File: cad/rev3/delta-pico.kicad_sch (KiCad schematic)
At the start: 69 parts, among them J1 Conn_01x02, J2 Conn_01x14, J3 Conn_01x04, J4 Conn_01x04, SW1 SW_SPDT, SW10 SW_Push, SW11 SW_Push, SW12 SW_Push, SW13 SW_Push, SW14 SW_Push, SW15 SW_Push, SW16 SW_Push, SW17 SW_Push, SW18 SW_Push, SW19 SW_Push, SW2 SW_Push, SW20 SW_Push, SW21 SW_Push, SW22 SW_Push, SW23 SW_Push, SW24 SW_Push, SW25 SW_Push, SW26 SW_Push, SW27 SW_Push, SW28 SW_Push, SW29 SW_Push, SW3 SW_Push, SW30 SW_Push, SW31 SW_Push, SW4 SW_Push, SW5 SW_Push, SW6 SW_Push, SW7 SW_Push, SW8 SW_Push, SW9 SW_Push, U1 PCF8574A, U2 PCF8574A, U3 Pico, U4 24LC16

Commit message: Fix footprint for new relative library path
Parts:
- U?: renamed from U3; footprint MCU_RaspberryPi_and_Boards:RPi_Pico_SMD -> RPi_Pico:RPi_Pico_SMD_TH
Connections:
- net 3V3: now also U?.36 (3V3)
- net CS: now also U?.6 (GPIO4)
- net DC: now also U?.7 (GPIO5)
- net DISPLAY_RESET: now also U?.9 (GPIO6)
- net GND: now also U?.3 (GND)
- net SCK: now also U?.4 (GPIO2)
- net SCL: now also U?.27 (GPIO21)
- net SDA: now also U?.26 (GPIO20)
- net SDI: now also U?.5 (GPIO3)
- net SDO: now also U?.1 (GPIO0)
- net SD_CS: now also U?.34 (GPIO28_ADC2)
- net VIN: now also U?.39 (VSYS)

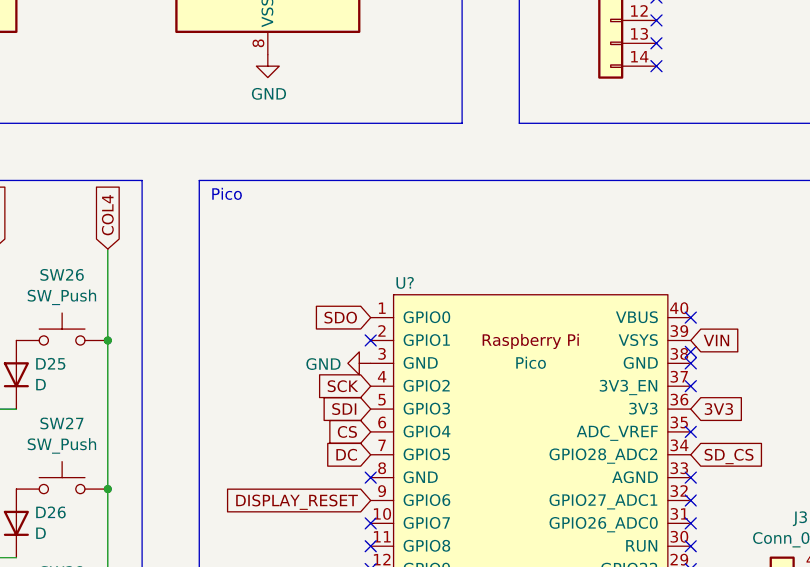
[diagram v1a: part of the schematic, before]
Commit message: Remove through-hole stuff from footprint, update board
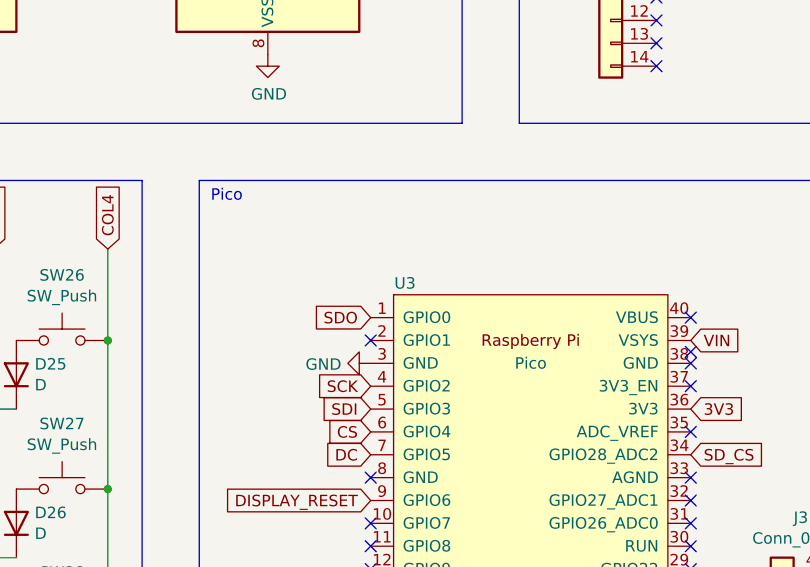
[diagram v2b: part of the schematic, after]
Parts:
- gave numbers to parts that had none: 1
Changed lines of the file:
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@@
 (kicad_sch (version 20210621) (generator eeschema)
   (paper "A4")
+  (junction (at 35.56 102.87) (diameter 0) (color 0 0 0 0))
+  (junction (at 45.72 128.27) (diameter 0) (color 0 0 0 0))
   (junction (at 48.26 168.91) (diameter 0) (color 0 0 0 0))
+  (junction (at 73.66 185.42) (diameter 0) (color 0 0 0 0))
+  (junction (at 48.26 185.42) (diameter 0) (color 0 0 0 0))
+  (junction (at 83.82 111.76) (diameter 0) (color 0 0 0 0))
+  (junction (at 45.72 144.78) (diameter 0) (color 0 0 0 0))
+  (junction (at 35.56 152.4) (diameter 0) (color 0 0 0 0))
+  (junction (at 45.72 111.76) (diameter 0) (color 0 0 0 0))
+  (junction (at 35.56 135.89) (diameter 0) (color 0 0 0 0))
+  (junction (at 48.26 102.87) (diameter 0) (color 0 0 0 0))
+  (junction (at 71.12 95.25) (diameter 0) (color 0 0 0 0))
+  (junction (at 45.72 95.25) (diameter 0) (color 0 0 0 0))
+  (junction (at 58.42 128.27) (diameter 0) (color 0 0 0 0))
+  (junction (at 73.66 152.4) (diameter 0) (color 0 0 0 0))
+  (junction (at 60.96 135.89) (diameter 0) (color 0 0 0 0))
+  (junction (at 73.66 102.87) (diameter 0) (color 0 0 0 0))
+  (junction (at 73.66 168.91) (diameter 0) (color 0 0 0 0))
+  (junction (at 58.42 111.76) (diameter 0) (color 0 0 0 0))
+  (junction (at 60.96 168.91) (diameter 0) (color 0 0 0 0))
+  (junction (at 96.52 95.25) (diameter 0) (color 0 0 0 0))
+  (junction (at 58.42 95.25) (diameter 0) (color 0 0 0 0))
+  (junction (at 48.26 119.38) (diameter 0) (color 0 0 0 0))
+  (junction (at 96.52 144.78) (diameter 0) (color 0 0 0 0))
+  (junction (at 45.72 161.29) (diameter 0) (color 0 0 0 0))
+  (junction (at 73.66 119.38) (diameter 0) (color 0 0 0 0))
+  (junction (at 119.38 170.18) (diameter 0) (color 0 0 0 0))
   (junction (at 83.82 161.29) (diameter 0) (color 0 0 0 0))
-  (junction (at 35.56 135.89) (diameter 0) (color 0 0 0 0))
+  (junction (at 48.26 152.4) (diameter 0) (color 0 0 0 0))
+  (junction (at 71.12 128.27) (diameter 0) (color 0 0 0 0))
+  (junction (at 96.52 161.29) (diameter 0) (color 0 0 0 0))
+  (junction (at 58.42 144.78) (diameter 0) (color 0 0 0 0))
+  (junction (at 83.82 95.25) (diameter 0) (color 0 0 0 0))
+  (junction (at 60.96 152.4) (diameter 0) (color 0 0 0 0))
+  (junction (at 71.12 111.76) (diameter 0) (color 0 0 0 0))
+  (junction (at 60.96 185.42) (diameter 0) (color 0 0 0 0))
+  (junction (at 58.42 161.29) (diameter 0) (color 0 0 0 0))
+  (junction (at 60.96 102.87) (diameter 0) (color 0 0 0 0))
+  (junction (at 96.52 111.76) (diameter 0) (color 0 0 0 0))
+  (junction (at 96.52 128.27) (diameter 0) (color 0 0 0 0))
+  (junction (at 71.12 144.78) (diameter 0) (color 0 0 0 0))
+  (junction (at 73.66 135.89) (diameter 0) (color 0 0 0 0))
+  (junction (at 71.12 161.29) (diameter 0) (color 0 0 0 0))
+  (junction (at 60.96 45.72) (diameter 0) (color 0 0 0 0))
+  (junction (at 35.56 185.42) (diameter 0) (color 0 0 0 0))
+  (junction (at 60.96 119.38) (diameter 0) (color 0 0 0 0))
+  (junction (at 60.96 48.26) (diameter 0) (color 0 0 0 0))
+  (junction (at 48.26 135.89) (diameter 0) (color 0 0 0 0))
   (junction (at 83.82 144.78) (diameter 0) (color 0 0 0 0))
-  (junction (at 73.66 185.42) (diameter 0) (color 0 0 0 0))
-  (junction (at 73.66 102.87) (diameter 0) (color 0 0 0 0))
-  (junction (at 58.42 128.27) (diameter 0) (color 0 0 0 0))
   (junction (at 83.82 128.27) (diameter 0) (color 0 0 0 0))
-  (junction (at 96.52 144.78) (diameter 0) (color 0 0 0 0))
-  (junction (at 35.56 185.42) (diameter 0) (color 0 0 0 0))
-  (junction (at 45.72 95.25) (diameter 0) (color 0 0 0 0))
-  (junction (at 35.56 102.87) (diameter 0) (color 0 0 0 0))
-  (junction (at 83.82 95.25) (diameter 0) (color 0 0 0 0))
-  (junction (at 96.52 161.29) (diameter 0) (color 0 0 0 0))
-  (junction (at 73.66 119.38) (diameter 0) (color 0 0 0 0))
-  (junction (at 60.96 102.87) (diameter 0) (color 0 0 0 0))
-  (junction (at 48.26 135.89) (diameter 0) (color 0 0 0 0))
-  (junction (at 60.96 168.91) (diameter 0) (color 0 0 0 0))
-  (junction (at 48.26 152.4) (diameter 0) (color 0 0 0 0))
-  (junction (at 71.12 111.76) (diameter 0) (color 0 0 0 0))
-  (junction (at 45.72 161.29) (diameter 0) (color 0 0 0 0))
   (junction (at 35.56 168.91) (diameter 0) (color 0 0 0 0))
-  (junction (at 58.42 161.29) (diameter 0) (color 0 0 0 0))
-  (junction (at 96.52 128.27) (diameter 0) (color 0 0 0 0))
-  (junction (at 60.96 135.89) (diameter 0) (color 0 0 0 0))
-  (junction (at 71.12 95.25) (diameter 0) (color 0 0 0 0))
-  (junction (at 48.26 119.38) (diameter 0) (color 0 0 0 0))
-  (junction (at 73.66 152.4) (diameter 0) (color 0 0 0 0))
   (junction (at 35.56 119.38) (diameter 0) (color 0 0 0 0))
-  (junction (at 73.66 135.89) (diameter 0) (color 0 0 0 0))
-  (junction (at 58.42 95.25) (diameter 0) (color 0 0 0 0))
-  (junction (at 35.56 152.4) (diameter 0) (color 0 0 0 0))
-  (junction (at 58.42 111.76) (diameter 0) (color 0 0 0 0))
-  (junction (at 119.38 170.18) (diameter 0) (color 0 0 0 0))
-  (junction (at 71.12 144.78) (diameter 0) (color 0 0 0 0))
-  (junction (at 58.42 144.78) (diameter 0) (color 0 0 0 0))
-  (junction (at 96.52 95.25) (diameter 0) (color 0 0 0 0))
-  (junction (at 45.72 128.27) (diameter 0) (color 0 0 0 0))
-  (junction (at 71.12 161.29) (diameter 0) (color 0 0 0 0))
-  (junction (at 48.26 185.42) (diameter 0) (color 0 0 0 0))
-  (junction (at 96.52 111.76) (diameter 0) (color 0 0 0 0))
-  (junction (at 60.96 48.26) (diameter 0) (color 0 0 0 0))
-  (junction (at 45.72 144.78) (diameter 0) (color 0 0 0 0))
-  (junction (at 60.96 45.72) (diameter 0) (color 0 0 0 0))
-  (junction (at 60.96 152.4) (diameter 0) (color 0 0 0 0))
-  (junction (at 83.82 111.76) (diameter 0) (color 0 0 0 0))
-  (junction (at 48.26 102.87) (diameter 0) (color 0 0 0 0))
-  (junction (at 60.96 119.38) (diameter 0) (color 0 0 0 0))
-  (junction (at 73.66 168.91) (diameter 0) (color 0 0 0 0))
-  (junction (at 71.12 128.27) (diameter 0) (color 0 0 0 0))
-  (junction (at 60.96 185.42) (diameter 0) (color 0 0 0 0))
-  (junction (at 45.72 111.76) (diameter 0) (color 0 0 0 0))
   (no_connect (at 161.29 113.03))
   (no_connect (at 161.29 120.65))
@@
   (symbol (lib_id "MCU_RaspberryPi_and_Boards:Pico") (at 143.51 116.84 0) (unit 1)
     (in_bom yes) (on_board yes)
-    (property "Reference" "U?" (id 0) (at 129.54 88.9 0))
+    (property "Reference" "U3" (id 0) (at 129.54 88.9 0))
     (property "Value" "Pico" (id 1) (at 143.51 97.79 0))
     (property "Footprint" "RPi_Pico:RPi_Pico_SMD_TH" (id 2) (at 143.51 116.84 90)
@@
   (symbol (lib_id "power:GND") (at 176.53 123.19 90) (unit 1)
     (in_bom yes) (on_board yes)
-    (property "Reference" "#PWR?" (id 0) (at 182.88 123.19 0)
+    (property "Reference" "#PWR0101" (id 0) (at 182.88 123.19 0)
       (effects (font (size 1.27 1.27)) hide)
     )
@@
       (reference "#PWR03") (unit 1) (value "GND") (footprint "")
     )
+    (path "/00000000-0000-0000-0000-0000613d20c7"
+      (reference "#PWR0101") (unit 1) (value "GND") (footprint "")
+    )
     (path "/00000000-0000-0000-0000-0000610b41f4"
       (reference "#PWR0104") (unit 1) (value "GND") (footprint "")
@@
       (reference "#PWR0116") (unit 1) (value "GND") (footprint "")
     )
-    (path "/00000000-0000-0000-0000-0000613d20c7"
-      (reference "#PWR?") (unit 1) (value "GND") (footprint "")
-    )
     (path "/00000000-0000-0000-0000-0000610dc627"
       (reference "D1") (unit 1) (value "D") (footprint "Diode_SMD:D_SOD-123")
@@
       (reference "U2") (unit 1) (value "PCF8574A") (footprint "Package_SO:SOIC-16W_7.5x10.3mm_P1.27mm")
     )
+    (path "/00000000-0000-0000-0000-0000610b053e"
+      (reference "U3") (unit 1) (value "Pico") (footprint "RPi_Pico:RPi_Pico_SMD_TH")
+    )
     (path "/00000000-0000-0000-0000-00006134770c"
       (reference "U4") (unit 1) (value "24LC16") (footprint "Package_SO:SOIC-8_3.9x4.9mm_P1.27mm")
     )
-    (path "/00000000-0000-0000-0000-0000610b053e"
-      (reference "U?") (unit 1) (value "Pico") (footprint "RPi_Pico:RPi_Pico_SMD_TH")
-    )
-  )
+  )

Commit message: Add a 6-pin "debug" port, in place of the expansion socket
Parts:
- removed J3: Conn_01x04, Connector_PinHeader_2.54mm:PinHeader_1x04_P2.54mm_Vertical, symbol Connector_Generic:Conn_01x04
- added J3: Conn_01x06, Connector_PinHeader_2.54mm:PinHeader_2x03_P2.54mm_Vertical, symbol Connector_Generic:Conn_01x06
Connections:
- net 3V3: now also J3.1 (Pin_1)
- net GND: now also J3.2 (Pin_2)
- net SCL: now also J3.3 (Pin_3)
- net SDA: now also J3.4 (Pin_4)
- net SWCLK: now reaches U3.41 (SWCLK)
- net SWCLK: now also J3.5 (Pin_5)
- net SWDIO: now reaches U3.43 (SWDIO)
- net SWDIO: now also J3.6 (Pin_6)
- no-connect marks 45 -> 43
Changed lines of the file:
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@@
   (no_connect (at 88.9 50.8))
   (no_connect (at 157.48 57.15))
-  (no_connect (at 140.97 146.05))
   (no_connect (at 63.5 55.88))
   (no_connect (at 161.29 105.41))
-  (no_connect (at 143.51 146.05))
   (no_connect (at 101.6 55.88))
   (no_connect (at 125.73 125.73))
@@
   (no_connect (at 125.73 138.43))
   (no_connect (at 127 50.8))
+  (no_connect (at 143.51 146.05))
   (no_connect (at 161.29 140.97))
   (no_connect (at 43.18 54.61))
@@
   (no_connect (at 161.29 92.71))
   (no_connect (at 161.29 123.19))
-  (no_connect (at 146.05 146.05))
   (no_connect (at 125.73 140.97))
   (no_connect (at 161.29 96.52))
@@
   (no_connect (at 161.29 97.79))
   (no_connect (at 157.48 54.61))
-  (polyline (pts (xy 106.68 77.47) (xy 185.42 77.47))
+  (polyline (pts (xy 106.68 77.47) (xy 189.23 77.47))
     (stroke (width 0) (type default) (color 0 0 0 0))
   )
@@
     (stroke (width 0) (type default) (color 0 0 0 0))
   )
-  (polyline (pts (xy 185.42 77.47) (xy 185.42 148.59))
+  (polyline (pts (xy 189.23 77.47) (xy 189.23 148.59))
     (stroke (width 0) (type default) (color 0 0 0 0))
   )
@@
     (stroke (width 0) (type default) (color 0 0 0 0))
   )
-  (polyline (pts (xy 185.42 148.59) (xy 106.68 148.59))
+  (polyline (pts (xy 189.23 148.59) (xy 106.68 148.59))
     (stroke (width 0) (type default) (color 0 0 0 0))
   )
@@
     )
   )
+  (global_label "SWDIO" (shape input) (at 146.05 146.05 0) (fields_autoplaced)
+    (effects (font (size 1.27 1.27)) (justify left))
+    (property "Intersheet References" "${INTERSHEET_REFS}" (id 0) (at 154.2404 145.9706 0)
+      (effects (font (size 1.27 1.27)) (justify left) hide)
+    )
+  )
   (global_label "COL2" (shape input) (at 71.12 85.09 90) (fields_autoplaced)
     (effects (font (size 1.27 1.27)) (justify left))
@@
     )
   )
+  (global_label "SWDIO" (shape input) (at 176.53 133.35 0) (fields_autoplaced)
+    (effects (font (size 1.27 1.27)) (justify left))
+    (property "Intersheet References" "${INTERSHEET_REFS}" (id 0) (at 184.7204 133.2706 0)
+      (effects (font (size 1.27 1.27)) (justify left) hide)
+    )
+  )
   (global_label "SCL" (shape input) (at 176.53 125.73 0) (fields_autoplaced)
     (effects (font (size 1.27 1.27)) (justify left))
@@
     )
   )
+  (global_label "SWCLK" (shape input) (at 140.97 146.05 180) (fields_autoplaced)
+    (effects (font (size 1.27 1.27)) (justify right))
+    (property "Intersheet References" "${INTERSHEET_REFS}" (id 0) (at 132.4168 145.9706 0)
+      (effects (font (size 1.27 1.27)) (justify right) hide)
+    )
+  )
   (global_label "ROW4" (shape input) (at 127 45.72 0) (fields_autoplaced)
     (effects (font (size 1.27 1.27)) (justify left))
@@
     (property "Intersheet References" "${INTERSHEET_REFS}" (id 0) (at 0 0 0)
       (effects (font (size 1.27 1.27)) hide)
+    )
+  )
+  (global_label "SWCLK" (shape input) (at 176.53 130.81 0) (fields_autoplaced)
+    (effects (font (size 1.27 1.27)) (justify left))
+    (property "Intersheet References" "${INTERSHEET_REFS}" (id 0) (at 185.0832 130.8894 0)
+      (effects (font (size 1.27 1.27)) (justify left) hide)
     )
   )
@@
     (pin "1")
   )
-  (symbol (lib_id "Connector_Generic:Conn_01x04") (at 171.45 125.73 180) (unit 1)
-    (in_bom yes) (on_board yes)
-    (property "Reference" "J3" (id 0) (at 173.5328 114.935 0))
-    (property "Value" "Conn_01x04" (id 1) (at 173.5328 117.2464 0))
-    (property "Footprint" "Connector_PinHeader_2.54mm:PinHeader_1x04_P2.54mm_Vertical" (id 2) (at 171.45 125.73 0)
+  (symbol (lib_id "Connector_Generic:Conn_01x06") (at 171.45 125.73 0) (mirror y) (unit 1)
+    (in_bom yes) (on_board yes) (fields_autoplaced)
+    (property "Reference" "J3" (id 0) (at 173.2915 115.4135 0))
+    (property "Value" "Conn_01x06" (id 1) (at 173.2915 118.1886 0))
+    (property "Footprint" "Connector_PinHeader_2.54mm:PinHeader_2x03_P2.54mm_Vertical" (id 2) (at 171.45 125.73 0)
       (effects (font (size 1.27 1.27)) hide)
     )
@@
     (pin "3")
     (pin "4")
+    (pin "5")
+    (pin "6")
   )
   (sheet_instances
@@
       (reference "J2") (unit 1) (value "Conn_01x14") (footprint "Connector_PinHeader_2.54mm:PinHeader_1x14_P2.54mm_Vertical")
     )
-    (path "/00000000-0000-0000-0000-000061542758"
-      (reference "J3") (unit 1) (value "Conn_01x04") (footprint "Connector_PinHeader_2.54mm:PinHeader_1x04_P2.54mm_Vertical")
+    (path "/75e094bf-41a7-4e89-9715-98b2e3d6e9d2"
+      (reference "J3") (unit 1) (value "Conn_01x06") (footprint "Connector_PinHeader_2.54mm:PinHeader_2x03_P2.54mm_Vertical")
     )
     (path "/00000000-0000-0000-0000-000061328a2d"

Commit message: Connect PCF8574 interrupt pins to GPIO 16/17
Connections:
- net COLINT: now reaches U3.21 (GPIO16)
- net COLINT: now also U1.13 (~{INT})
- net ROWINT: now reaches U3.22 (GPIO17)
- net ROWINT: now also U2.13 (~{INT})
- no-connect marks 43 -> 39
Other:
- note added: "Internal pullups should be fine"
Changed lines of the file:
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@@
   (no_connect (at 88.9 50.8))
   (no_connect (at 157.48 57.15))
-  (no_connect (at 63.5 55.88))
   (no_connect (at 161.29 105.41))
-  (no_connect (at 101.6 55.88))
   (no_connect (at 125.73 125.73))
   (no_connect (at 125.73 133.35))
@@
   (no_connect (at 127 50.8))
   (no_connect (at 143.51 146.05))
-  (no_connect (at 161.29 140.97))
   (no_connect (at 43.18 54.61))
   (no_connect (at 125.73 110.49))
@@
   (no_connect (at 161.29 115.57))
   (no_connect (at 157.48 62.23))
-  (no_connect (at 161.29 138.43))
   (no_connect (at 125.73 118.11))
   (no_connect (at 161.29 92.71))
@@
     (stroke (width 0) (type default) (color 0 0 0 0))
   )
+  (text "Internal pullups\nshould be fine" (at 171.45 142.24 0)
+    (effects (font (size 1.27 1.27) italic) (justify left bottom))
+  )
   (text "Display" (at 143.51 19.05 0)
     (effects (font (size 1.27 1.27)) (justify left bottom))
@@
     )
   )
+  (global_label "ROWINT" (shape input) (at 101.6 55.88 270) (fields_autoplaced)
+    (effects (font (size 1.27 1.27)) (justify right))
+    (property "Intersheet References" "${INTERSHEET_REFS}" (id 0) (at 101.5206 65.159 90)
+      (effects (font (size 1.27 1.27)) (justify right) hide)
+    )
+  )
   (global_label "3V3" (shape input) (at 101.6 45.72 180) (fields_autoplaced)
     (effects (font (size 1.27 1.27)) (justify right))
@@
     )
   )
+  (global_label "ROWINT" (shape input) (at 161.29 138.43 0) (fields_autoplaced)
+    (effects (font (size 1.27 1.27)) (justify left))
+    (property "Intersheet References" "${INTERSHEET_REFS}" (id 0) (at 170.569 138.5094 0)
+      (effects (font (size 1.27 1.27)) (justify left) hide)
+    )
+  )
   (global_label "3V3" (shape input) (at 101.6 48.26 180) (fields_autoplaced)
     (effects (font (size 1.27 1.27)) (justify right))
@@
     (property "Intersheet References" "${INTERSHEET_REFS}" (id 0) (at 0 0 0)
       (effects (font (size 1.27 1.27)) hide)
+    )
+  )
+  (global_label "COLINT" (shape input) (at 161.29 140.97 0) (fields_autoplaced)
+    (effects (font (size 1.27 1.27)) (justify left))
+    (property "Intersheet References" "${INTERSHEET_REFS}" (id 0) (at 170.1456 141.0494 0)
+      (effects (font (size 1.27 1.27)) (justify left) hide)
     )
   )
@@
     )
   )
+  (global_label "COLINT" (shape input) (at 63.5 55.88 270) (fields_autoplaced)
+    (effects (font (size 1.27 1.27)) (justify right))
+    (property "Intersheet References" "${INTERSHEET_REFS}" (id 0) (at 63.4206 64.7356 90)
+      (effects (font (size 1.27 1.27)) (justify right) hide)
+    )
+  )

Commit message: Break out some bonus GPIO and VIN
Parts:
- added J5: Conn_01x03, Connector_PinHeader_2.54mm:PinHeader_1x03_P2.54mm_Vertical, symbol Connector_Generic:Conn_01x03
- J3: value Conn_01x06 -> Conn_01x08; footprint Connector_PinHeader_2.54mm:PinHeader_2x03_P2.54mm_Vertical -> Connector_PinHeader_2.54mm:PinHeader_2x04_P2.54mm_Vertical; symbol Connector_Generic:Conn_01x06 -> Connector_Generic:Conn_01x08
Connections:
- net 3V3: now also J3.3 (Pin_3); no longer J3.1 (Pin_1)
- net GND: now also J3.4 (Pin_4), J5.3 (Pin_3); no longer J3.2 (Pin_2)
- net SCL: now also J3.5 (Pin_5); no longer J3.3 (Pin_3)
- net SDA: now also J3.6 (Pin_6); no longer J3.4 (Pin_4)
- net SWCLK: now also J3.7 (Pin_7); no longer J3.5 (Pin_5)
- net SWDIO: now also J3.8 (Pin_8); no longer J3.6 (Pin_6)
- net VIN: now also J5.2 (Pin_2)
- net GP18: now reaches U3.24 (GPIO18)
- net GP18: now also J3.2 (Pin_2)
- net GP19: now reaches U3.25 (GPIO19)
- net GP19: now also J3.1 (Pin_1)
- net RAWVIN: now reaches J1.1 (Pin_1), SW1.2 (B)
- net RAWVIN: now also J5.1 (Pin_1)
- no-connect marks 39 -> 37
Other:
- note added: "Debug Headers"
